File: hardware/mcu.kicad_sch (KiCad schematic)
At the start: 63 parts, among them J501 SBH11-NBPC-D05-SM-BK, J502 PRPC006SAAN-RC, J503 PRPC006SAAN-RC, J504 PRPC006SAAN-RC, J505 PRPC006SAAN-RC, J506 PRPC006SAAN-RC, J507 PRPC006SAAN-RC, J508 PRPC006SAAN-RC, J509 PRPC001DAAN-RC, U501 STM32L552CEU6, U502 AT25SF081B-MAHB-T, Y501 ECS-160-9-37-CKM-TR3, Y502 ABS05-32.768KHZ-9-T

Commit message: HW: Add battery detection
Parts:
- added Q501: BSS806NH, Package_TO_SOT_SMD:SOT-23-3, symbol Transistor_FET:Q_NMOS_GSD
- added R501: 2.2 kΩ, perfect_footprints:R_0402_1005Metric, symbol Device:R
- added R502, R505: 180 kΩ, perfect_footprints:R_0402_1005Metric, symbol Device:R
- added R508: 330 Ω, perfect_footprints:R_0402_1005Metric, symbol Device:R
- added TP501, TP502, TP503: TestPoint, TestPoint:TestPoint_Pad_D1.0mm, symbol Connector:TestPoint
- renumbered R501 to R503, R502 to R504, R503 to R506, R504 to R507, R505 to R509, R506 to R510, R507 to R511, R508 to R512, R509 to R513, R510 to R514, R511 to R515, R512 to R516, R513 to R517, R514 to R518, R515 to R519, R516 to R520, R517 to R521, R518 to R522, R519 to R523, R520 to R524, R521 to R525, TP501 to TP504, TP502 to TP505, TP503 to TP506, TP504 to TP507, TP505 to TP508, TP506 to TP509, TP507 to TP510, TP508 to TP511, TP509 to TP512
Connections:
- net GND: now also J507.5 (Pin_5), Q501.2 (S), R502.2
- net V_3V3: now also R505.1
- net GPIO_PA1 renamed BAT_DET
- net BAT_DET: now also R508.1, TP503.1; no longer J507.5 (Pin_5)
- new net: Q501.3 (D), R505.2, R508.2, TP502.1
- new net: Q501.1 (G), R501.2, R502.1, TP501.1
- new net BAT_DET_IN: R501.1
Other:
- moved on the sheet: R503, R504, R506, R507

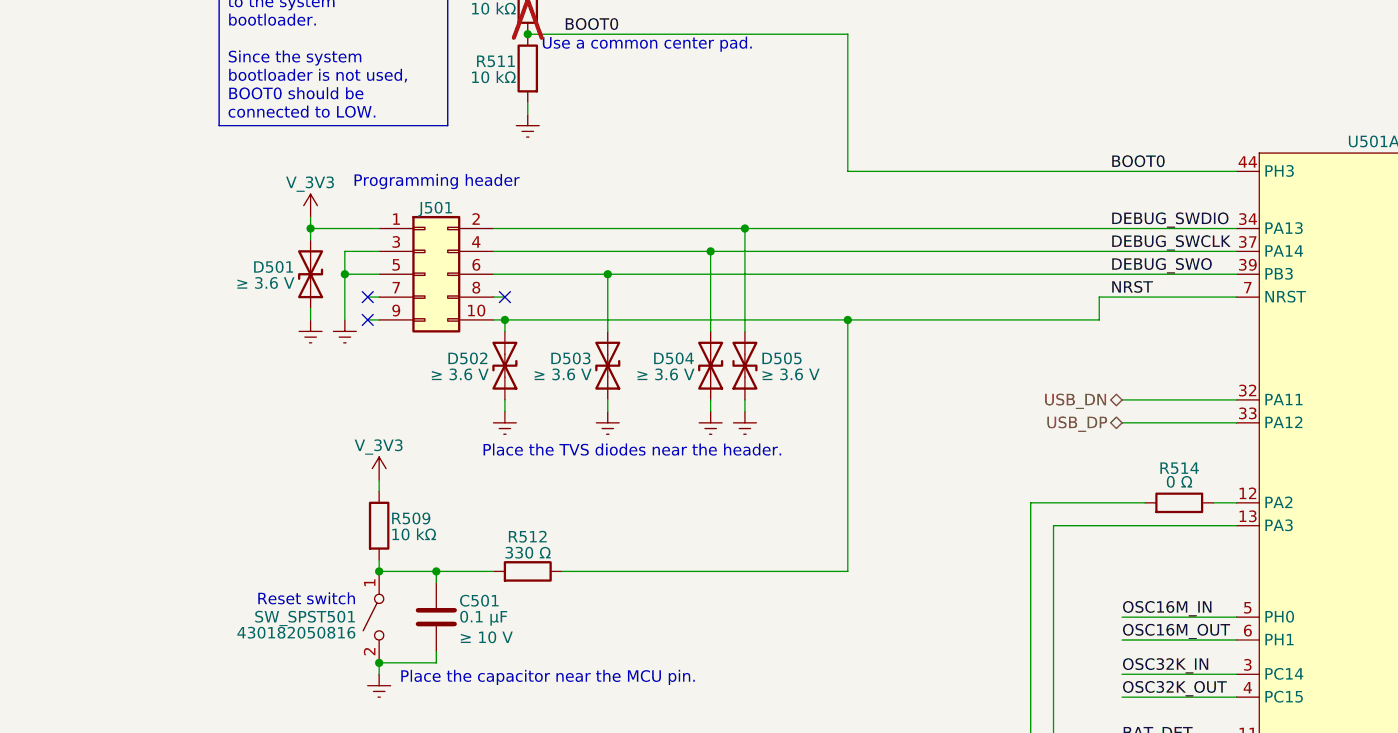
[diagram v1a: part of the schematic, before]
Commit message: HW: Use TC2050 for debugging
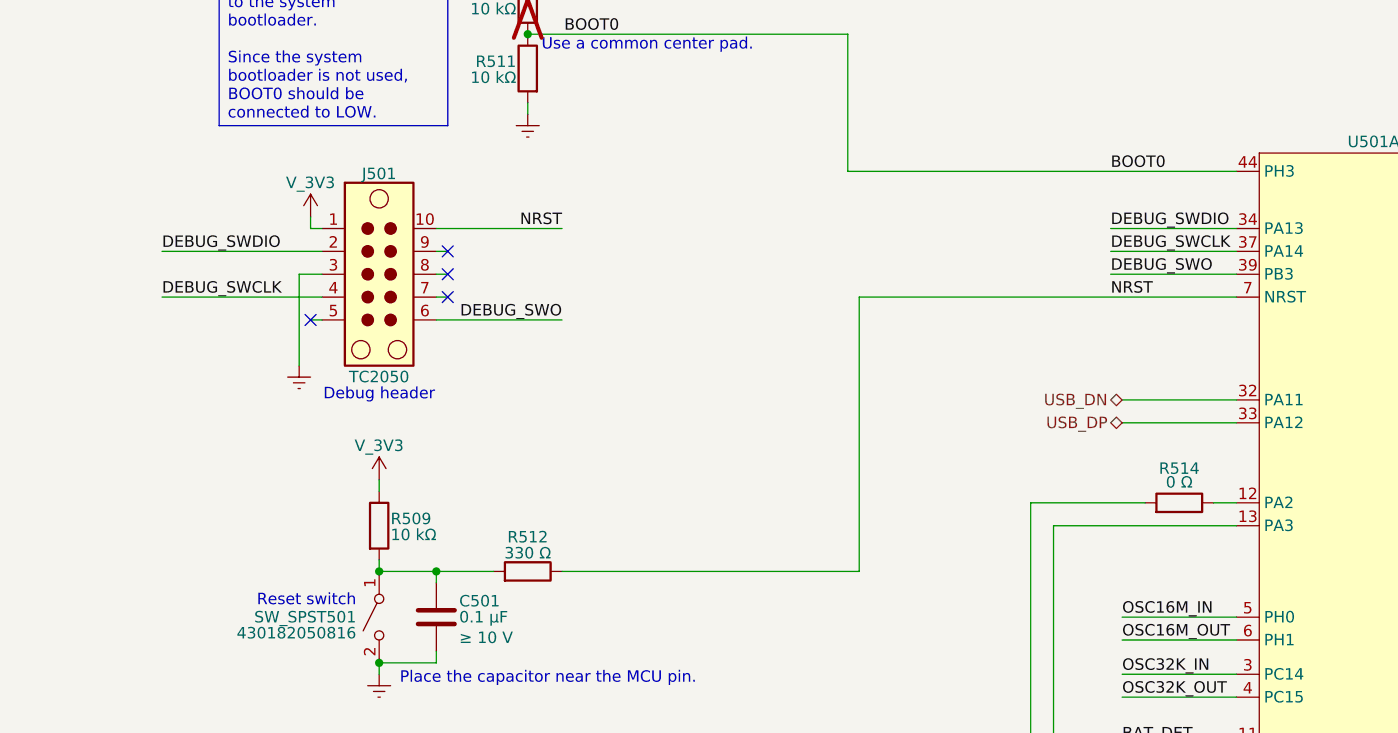
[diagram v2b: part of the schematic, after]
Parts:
- removed D501, D502, D503, D504, D505: DF2B5M4CT,L3F, Diode_SMD:D_SOD-882D, symbol Device:D_TVS
- removed J501: SBH11-NBPC-D05-SM-BK, Connector_IDC:IDC-Header_2x05_P2.54mm_Vertical, symbol Connector_Generic:Conn_02x05_Odd_Even
- added J501: TC2050, Connector:Tag-Connect_TC2050-IDC-NL_2x05_P1.27mm_Vertical_with_bottom_clip, symbol Connector:TC2050
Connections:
- net DEBUG_SWCLK: now also J501.4
- net DEBUG_SWDIO: now also J501.2
- net DEBUG_SWO: now also J501.6
- net GND: now also J501.3
- net NRST: now also J501.10
- net V_3V3: now also J501.1
- no-connect marks 7 -> 8
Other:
- note added: "Debug header"
- note removed: "Place the TVS diodes near the header."
- note removed: "Programming header"

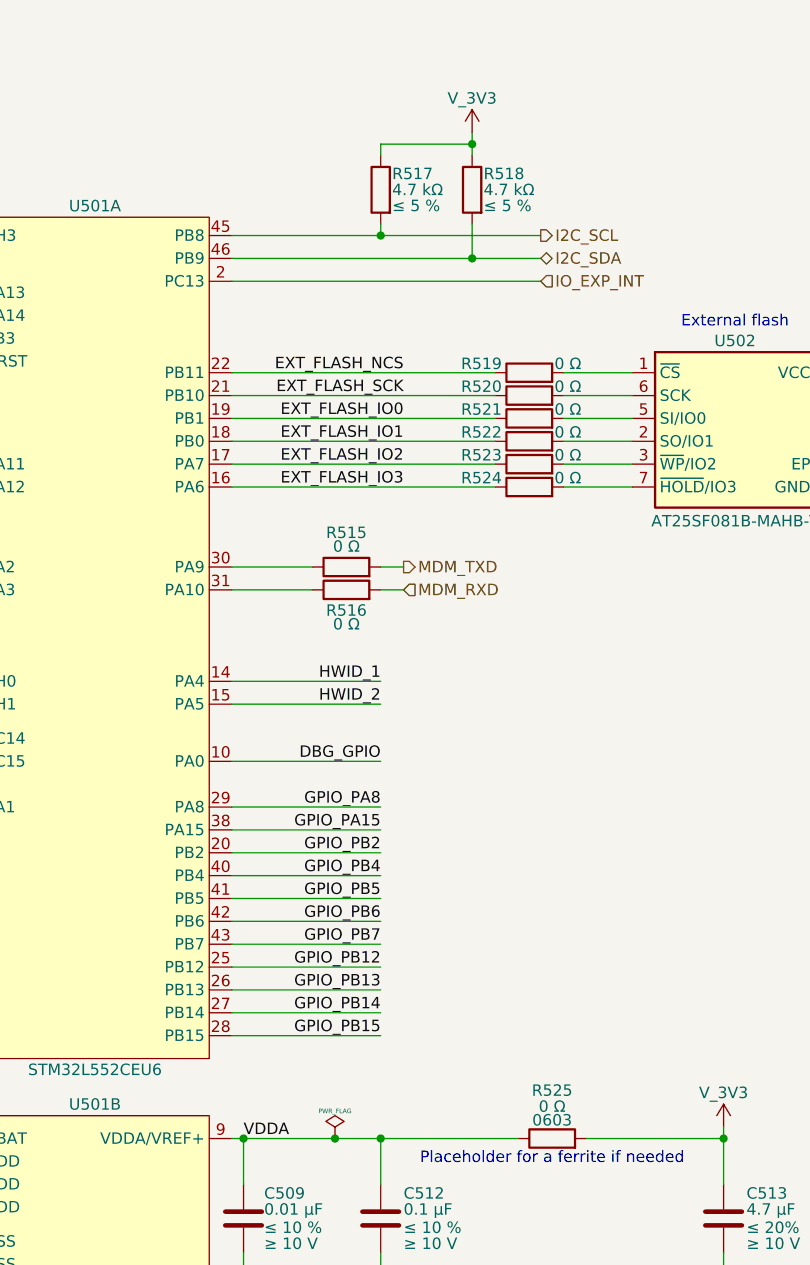
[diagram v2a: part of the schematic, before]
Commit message: HW: Move MDM_RXD termination resistor
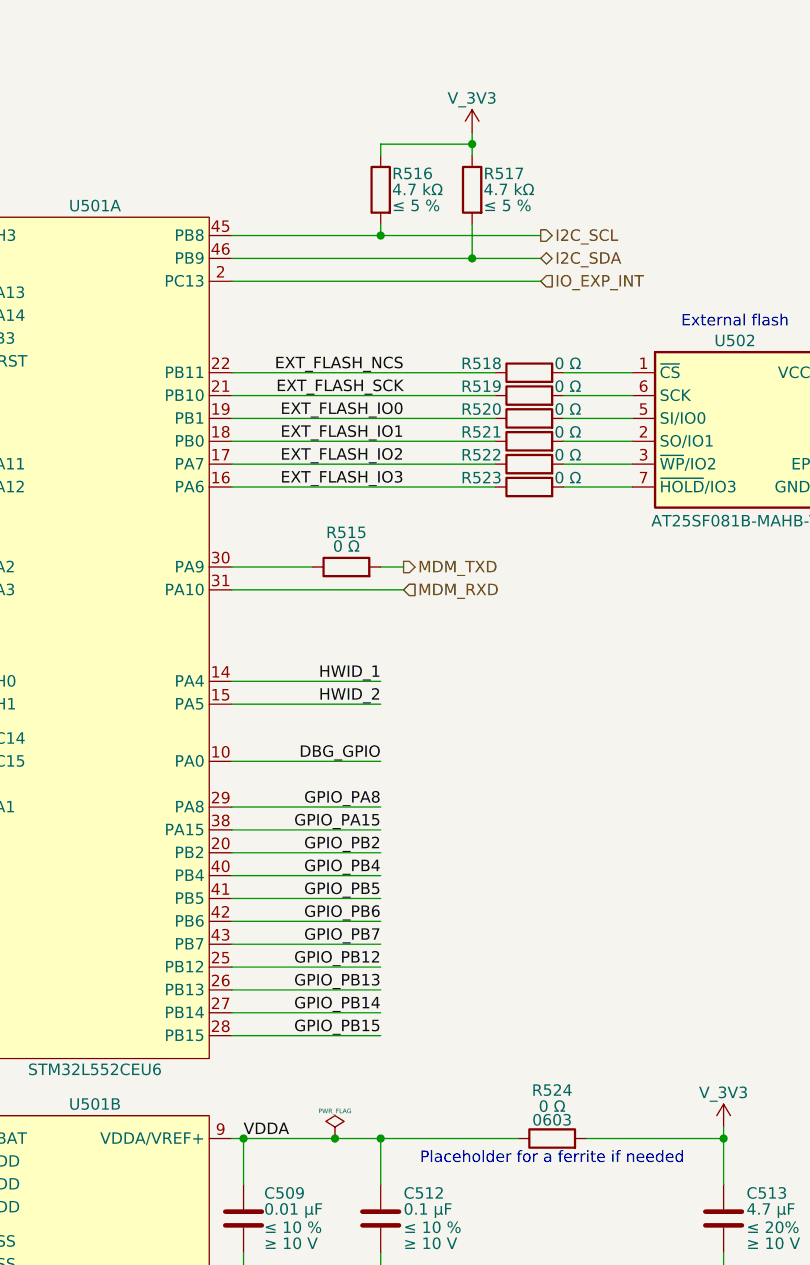
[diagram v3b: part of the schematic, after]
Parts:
- removed R516: 0 Ω, perfect_footprints:R_0402_1005Metric, symbol Device:R
- renumbered R517 to R516, R518 to R517, R519 to R518, R520 to R519, R521 to R520, R522 to R521, R523 to R522, R524 to R523, R525 to R524
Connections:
- net MDM_RXD: now also U501.31 (PA10)
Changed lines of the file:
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@@
 	(wire
 		(pts
-			(xy 241.3 123.19) (xy 243.84 123.19)
-		)
-		(stroke
-			(width 0)
-			(type default)
-		)
-	)
-	(wire
-		(pts
 			(xy 397.51 91.44) (xy 394.97 91.44)
 		)
@@
 	(wire
 		(pts
-			(xy 224.79 123.19) (xy 233.68 123.19)
+			(xy 224.79 123.19) (xy 243.84 123.19)
 		)
 		(stroke
@@
 		(on_board yes)
 		(dnp no)
-		(property "Reference" "R523"
+		(property "Reference" "R522"
 			(at 254.762 108.966 90)
 			(effects
@@
 			(project "iida_devkit"
 				(path "/b12a6e25-97fb-4aba-bc96-af8db389bb9a/6dd8d741-3080-458c-a4f5-a05a3905bb8a"
-					(reference "R523")
+					(reference "R522")
 					(unit 1)
 				)
@@
 		(on_board yes)
 		(dnp no)
-		(property "Reference" "R519"
+		(property "Reference" "R518"
 			(at 254.762 98.806 90)
 			(effects
@@
 			(project "iida_devkit"
 				(path "/b12a6e25-97fb-4aba-bc96-af8db389bb9a/6dd8d741-3080-458c-a4f5-a05a3905bb8a"
-					(reference "R519")
+					(reference "R518")
 					(unit 1)
 				)
@@
 		(on_board yes)
 		(dnp no)
-		(property "Reference" "R518"
+		(property "Reference" "R517"
 			(at 252.73 76.962 0)
 			(effects
@@
 			(project "iida_devkit"
 				(path "/b12a6e25-97fb-4aba-bc96-af8db389bb9a/6dd8d741-3080-458c-a4f5-a05a3905bb8a"
-					(reference "R518")
+					(reference "R517")
 					(unit 1)
 				)
@@
 		(on_board yes)
 		(dnp no)
-		(property "Reference" "R525"
+		(property "Reference" "R524"
 			(at 260.35 178.816 90)
 			(effects
@@
 			(project "iida_devkit"
 				(path "/b12a6e25-97fb-4aba-bc96-af8db389bb9a/6dd8d741-3080-458c-a4f5-a05a3905bb8a"
-					(reference "R525")
+					(reference "R524")
 					(unit 1)
 				)
@@
 		(on_board yes)
 		(dnp no)
-		(property "Reference" "R520"
+		(property "Reference" "R519"
 			(at 254.762 101.346 90)
 			(effects
@@
 			(project "iida_devkit"
 				(path "/b12a6e25-97fb-4aba-bc96-af8db389bb9a/6dd8d741-3080-458c-a4f5-a05a3905bb8a"
-					(reference "R520")
+					(reference "R519")
 					(unit 1)
 				)
@@
 		(on_board yes)
 		(dnp no)
-		(property "Reference" "R524"
+		(property "Reference" "R523"
 			(at 254.762 111.506 90)
 			(effects
@@
 			(project "iida_devkit"
 				(path "/b12a6e25-97fb-4aba-bc96-af8db389bb9a/6dd8d741-3080-458c-a4f5-a05a3905bb8a"
-					(reference "R524")
+					(reference "R523")
 					(unit 1)
 				)
@@
 		(on_board yes)
 		(dnp no)
-		(property "Reference" "R522"
+		(property "Reference" "R521"
 			(at 254.762 106.426 90)
 			(effects
@@
 			(project "iida_devkit"
 				(path "/b12a6e25-97fb-4aba-bc96-af8db389bb9a/6dd8d741-3080-458c-a4f5-a05a3905bb8a"
-					(reference "R522")
+					(reference "R521")
 					(unit 1)
 				)
@@
 		(on_board yes)
 		(dnp no)
-		(property "Reference" "R517"
+		(property "Reference" "R516"
 			(at 242.57 76.962 0)
 			(effects
@@
 			(project "iida_devkit"
 				(path "/b12a6e25-97fb-4aba-bc96-af8db389bb9a/6dd8d741-3080-458c-a4f5-a05a3905bb8a"
-					(reference "R517")
+					(reference "R516")
 					(unit 1)
 				)
@@
 	(symbol
 		(lib_id "Device:R")
-		(at 237.49 123.19 90)
-		(unit 1)
-		(exclude_from_sim no)
-		(in_bom yes)
-		(on_board yes)
-		(dnp no)
-		(property "Reference" "R516"
-			(at 237.49 125.476 90)
-			(effects
-				(font
-					(size 1.27 1.27)
-				)
-			)
-		)
-		(property "Value" "0 Ω"
-			(at 237.49 127 90)
-			(effects
-				(font
-					(size 1.27 1.27)
-				)
-			)
-		)
-		(property "Footprint" "perfect_footprints:R_0402_1005Metric"
-			(at 237.49 124.968 90)
-			(effects
-				(font
-					(size 1.27 1.27)
-				)
-				(hide yes)
-			)
-		)
-		(property "Datasheet" "~"
-			(at 237.49 123.19 0)
-			(effects
-				(font
-					(size 1.27 1.27)
-				)
-				(hide yes)
-			)
-		)
-		(property "Description" ""
-			(at 237.49 123.19 0)
-			(effects
-				(font
-					(size 1.27 1.27)
-				)
-				(hide yes)
-			)
-		)
-		(property "Manufacturer" "Würth Elektronik"
-			(at 237.49 123.19 0)
-			(effects
-				(font
-					(size 1.27 1.27)
-				)
-				(hide yes)
-			)
-		)
-		(property "Footprint review check" "+"
-			(at 237.49 123.19 0)
-			(effects
-				(font
-					(size 1.27 1.27)
-				)
-				(hide yes)
-			)
-		)
-		(property "MPN" "560112110001"
-			(at 237.49 123.19 0)
-			(effects
-				(font
-					(size 1.27 1.27)
-				)
-				(hide yes)
-			)
-		)
-		(property "Size" "0402"
-			(at 237.49 123.19 0)
-			(effects
-				(font
-					(size 1.27 1.27)
-				)
-				(hide yes)
-			)
-		)
-		(property "DigiKey Part Number" "732-560112110001CT-ND"
-			(at 237.49 123.19 90)
-			(effects
-				(font
-					(size 1.27 1.27)
-				)
-				(hide yes)
-			)
-		)
-		(property "Power" ""
-			(at 237.49 123.19 90)
-			(effects
-				(font
-					(size 1.27 1.27)
-				)
-				(hide yes)
-			)
-		)
-		(pin "2"
-		)
-		(pin "1"
-		)
-		(instances
-			(project "iida_devkit"
-				(path "/b12a6e25-97fb-4aba-bc96-af8db389bb9a/6dd8d741-3080-458c-a4f5-a05a3905bb8a"
-					(reference "R516")
-					(unit 1)
-				)
-			)
-		)
-	)
-	(symbol
-		(lib_id "Device:R")
 		(at 257.81 104.14 90)
 		(unit 1)
@@
 		(on_board yes)
 		(dnp no)
-		(property "Reference" "R521"
+		(property "Reference" "R520"
 			(at 254.762 103.886 90)
 			(effects
@@
 			(project "iida_devkit"
 				(path "/b12a6e25-97fb-4aba-bc96-af8db389bb9a/6dd8d741-3080-458c-a4f5-a05a3905bb8a"
-					(reference "R521")
+					(reference "R520")
 					(unit 1)
 				)

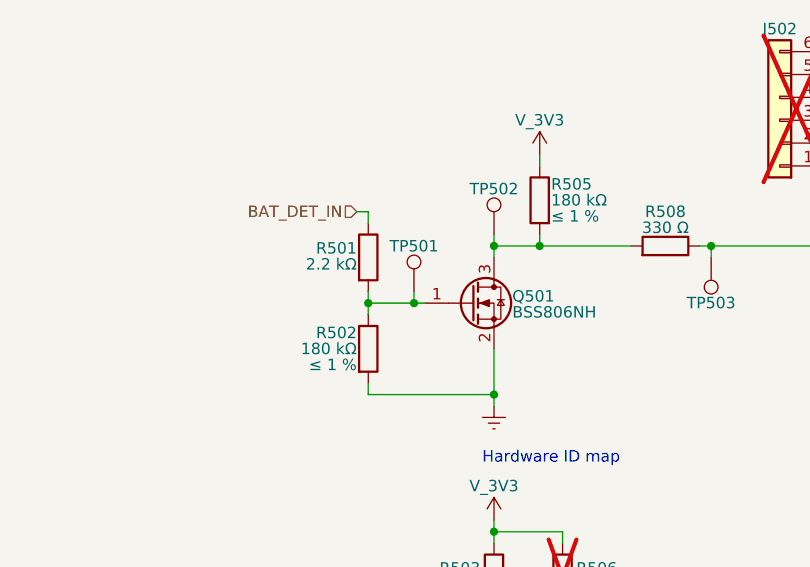
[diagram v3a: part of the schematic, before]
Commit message: HW: Refactor modem power fets
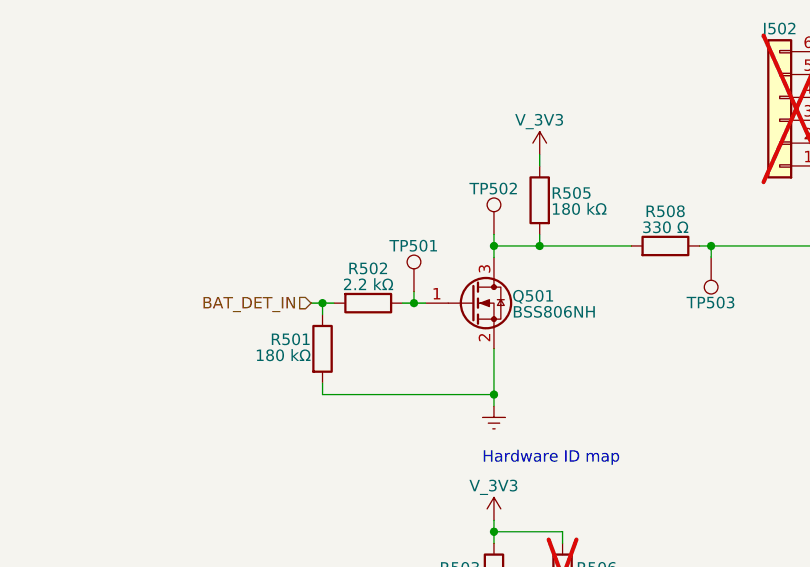
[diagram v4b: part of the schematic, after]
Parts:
- removed R501: 2.2 kΩ, perfect_footprints:R_0402_1005Metric, symbol Device:R
- added R502: 2.2 kΩ, perfect_footprints:R_0402_1005Metric, symbol Device:R
- renumbered R502 to R501
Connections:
- net BAT_DET_IN: now also R501.1, R502.2
- net at Q501.1 (G), TP501.1: now also R502.1; no longer R501.1
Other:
- moved on the sheet: R501

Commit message: HW: Add bandpass filter to PCB antenna
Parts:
- R524: DigiKey Part Number 732-560112116001CT-ND -> (none); MPN 560112116001 -> (none); Manufacturer Würth Elektronik -> (none)
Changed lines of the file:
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@@
 			)
 		)
-		(property "Manufacturer" "Würth Elektronik"
+		(property "Manufacturer" ""
 			(at 260.35 184.15 0)
 			(effects
@@
 			)
 		)
-		(property "MPN" "560112116001"
+		(property "MPN" ""
 			(at 260.35 184.15 0)
 			(effects
@@
 			)
 		)
-		(property "DigiKey Part Number" "732-560112116001CT-ND"
+		(property "DigiKey Part Number" ""
 			(at 260.35 184.15 90)
 			(effects
